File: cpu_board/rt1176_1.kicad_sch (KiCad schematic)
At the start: 81 parts, among them U2 MIMXRT1176, Y3 24.0mHz

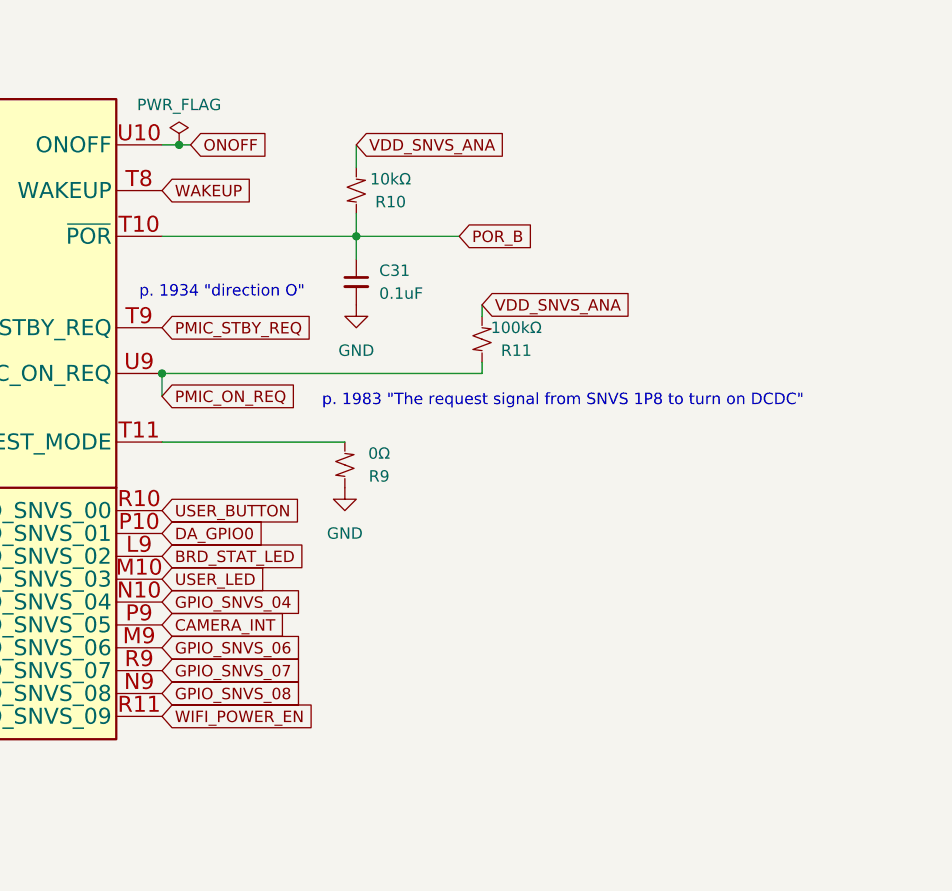
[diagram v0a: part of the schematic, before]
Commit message: clean up board2board connector and organize TODOs
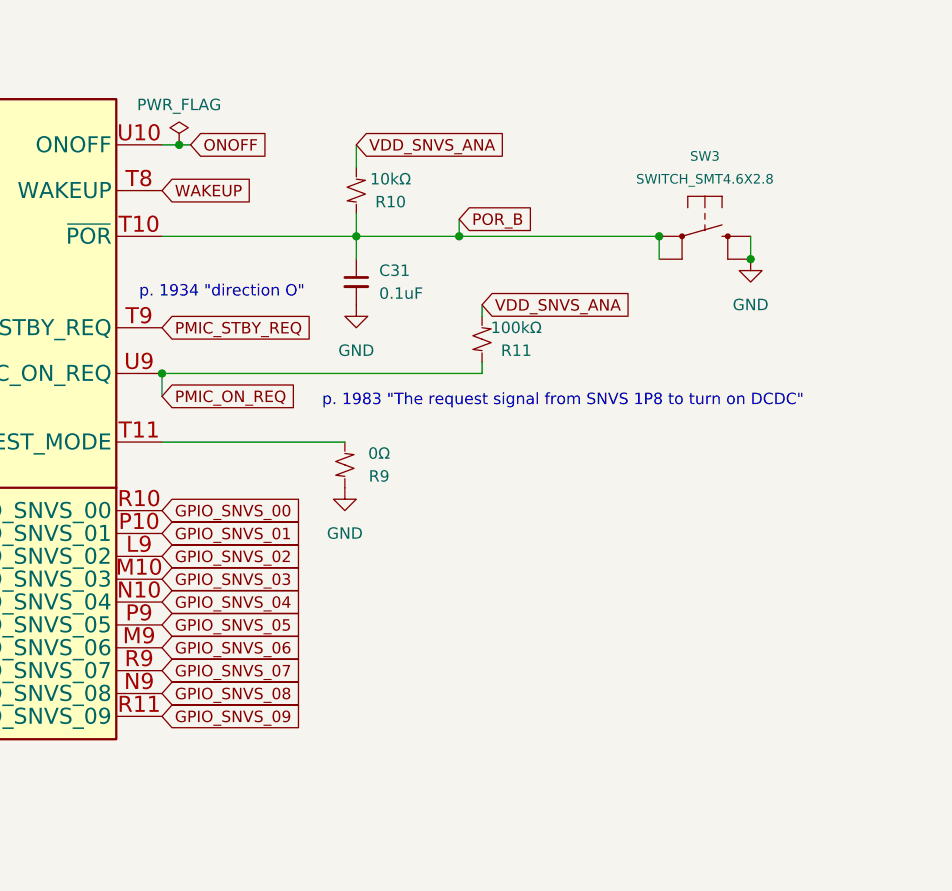
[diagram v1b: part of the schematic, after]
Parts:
- added SW3: SWITCH_SMT4.6X2.8, symbol pycubed_mainboard:SWITCH_SMT4.6X2.8
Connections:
- net GND: now also SW3.B (S), SW3.B' (S1)
- net POR_B: now also SW3.A (P), SW3.A' (P1)
- net BRD_STAT_LED renamed GPIO_SNVS_02
- net CAMERA_INT renamed GPIO_SNVS_05
- net DA_GPIO0 renamed GPIO_SNVS_01
- net USER_BUTTON renamed GPIO_SNVS_00
- net USER_LED renamed GPIO_SNVS_03
- net WIFI_POWER_EN renamed GPIO_SNVS_09
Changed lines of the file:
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@@
   (junction (at 157.48 182.88) (diameter 0) (color 0 0 0 0)
   )
+  (junction (at 304.165 45.72) (diameter 0) (color 0 0 0 0)
+  )
   (junction (at 182.88 48.26) (diameter 0) (color 0 0 0 0)
   )
@@
   (junction (at 152.4 157.48) (diameter 0) (color 0 0 0 0)
   )
+  (junction (at 314.325 48.26) (diameter 0) (color 0 0 0 0)
+  )
   (junction (at 35.56 259.08) (diameter 0) (color 0 0 0 0)
   )
@@
   (junction (at 35.56 241.3) (diameter 0) (color 0 0 0 0)
   )
+  (junction (at 281.94 45.72) (diameter 0) (color 0 0 0 0)
+  )
   (junction (at 66.04 251.46) (diameter 0) (color 0 0 0 0)
   )
@@
     (stroke (width 0) (type default))
   )
+  (wire (pts (xy 281.94 43.815) (xy 281.94 45.72))
+    (stroke (width 0) (type default))
+  )
   (wire (pts (xy 271.78 180.34) (xy 281.94 180.34))
     (stroke (width 0) (type default))
@@
     (stroke (width 0) (type default))
   )
+  (wire (pts (xy 281.94 45.72) (xy 304.165 45.72))
+    (stroke (width 0) (type default))
+  )
   (wire (pts (xy 320.04 129.54) (xy 330.2 129.54))
     (stroke (width 0) (type default))
@@
     (stroke (width 0) (type default))
   )
+  (wire (pts (xy 314.325 45.72) (xy 314.325 48.26))
+    (stroke (width 0) (type default))
+  )
   (wire (pts (xy 246.38 208.28) (xy 246.38 210.82))
     (stroke (width 0) (type default))
@@
     (stroke (width 0) (type default))
   )
+  (wire (pts (xy 304.165 45.72) (xy 304.165 48.26))
+    (stroke (width 0) (type default))
+  )
   (wire (pts (xy 152.4 157.48) (xy 162.56 157.48))
     (stroke (width 0) (type default))
@@
     )
   )
-  (global_label "USER_BUTTON" (shape input) (at 248.92 76.2 0) (fields_autoplaced)
+  (global_label "GPIO_SNVS_00" (shape input) (at 248.92 76.2 0) (fields_autoplaced)
     (effects (font (size 1.27 1.27)) (justify left))
-    (property "Intersheetrefs" "${INTERSHEET_REFS}" (at 265.0285 76.2 0)
+    (property "Intersheetrefs" "${INTERSHEET_REFS}" (at 265.5728 76.2 0)
       (effects (font (size 1.27 1.27)) (justify left) hide)
     )
   )
-  (global_label "CAMERA_INT" (shape input) (at 248.92 88.9 0) (fields_autoplaced)
+  (global_label "GPIO_SNVS_05" (shape input) (at 248.92 88.9 0) (fields_autoplaced)
     (effects (font (size 1.27 1.27)) (justify left))
-    (property "Intersheetrefs" "${INTERSHEET_REFS}" (at 263.0933 88.9 0)
+    (property "Intersheetrefs" "${INTERSHEET_REFS}" (at 265.5728 88.9 0)
       (effects (font (size 1.27 1.27)) (justify left) hide)
     )
@@
     )
   )
-  (global_label "DA_GPIO0" (shape input) (at 248.92 78.74 0) (fields_autoplaced)
+  (global_label "GPIO_SNVS_01" (shape input) (at 248.92 78.74 0) (fields_autoplaced)
     (effects (font (size 1.27 1.27)) (justify left))
-    (property "Intersheetrefs" "${INTERSHEET_REFS}" (at 260.9162 78.74 0)
+    (property "Intersheetrefs" "${INTERSHEET_REFS}" (at 265.5728 78.74 0)
       (effects (font (size 1.27 1.27)) (justify left) hide)
     )
@@
     )
   )
-  (global_label "WIFI_POWER_EN" (shape input) (at 248.92 99.06 0) (fields_autoplaced)
+  (global_label "GPIO_SNVS_09" (shape input) (at 248.92 99.06 0) (fields_autoplaced)
     (effects (font (size 1.27 1.27)) (justify left))
-    (property "Intersheetrefs" "${INTERSHEET_REFS}" (at 266.5404 99.06 0)
+    (property "Intersheetrefs" "${INTERSHEET_REFS}" (at 265.5728 99.06 0)
       (effects (font (size 1.27 1.27)) (justify left) hide)
     )
@@
     )
   )
-  (global_label "BRD_STAT_LED" (shape input) (at 248.92 81.28 0) (fields_autoplaced)
+  (global_label "GPIO_SNVS_02" (shape input) (at 248.92 81.28 0) (fields_autoplaced)
     (effects (font (size 1.27 1.27)) (justify left))
-    (property "Intersheetrefs" "${INTERSHEET_REFS}" (at 265.3308 81.28 0)
+    (property "Intersheetrefs" "${INTERSHEET_REFS}" (at 265.5728 81.28 0)
       (effects (font (size 1.27 1.27)) (justify left) hide)
     )
@@
     )
   )
-  (global_label "POR_B" (shape input) (at 281.94 45.72 0) (fields_autoplaced)
+  (global_label "POR_B" (shape input) (at 281.94 43.815 0) (fields_autoplaced)
     (effects (font (size 1.27 1.27)) (justify left))
-    (property "Intersheetrefs" "${INTERSHEET_REFS}" (at 291.0333 45.72 0)
+    (property "Intersheetrefs" "${INTERSHEET_REFS}" (at 291.0333 43.815 0)
       (effects (font (size 1.27 1.27)) (justify left) hide)
     )
@@
     )
   )
-  (global_label "USER_LED" (shape input) (at 248.92 83.82 0) (fields_autoplaced)
+  (global_label "GPIO_SNVS_03" (shape input) (at 248.92 83.82 0) (fields_autoplaced)
     (effects (font (size 1.27 1.27)) (justify left))
-    (property "Intersheetrefs" "${INTERSHEET_REFS}" (at 261.2789 83.82 0)
+    (property "Intersheetrefs" "${INTERSHEET_REFS}" (at 265.5728 83.82 0)
       (effects (font (size 1.27 1.27)) (justify left) hide)
     )
@@
     )
   )
+  (symbol (lib_id "power:GND") (at 314.325 48.26 0) (unit 1)
+    (in_bom yes) (on_board yes) (dnp no) (fields_autoplaced)
+    (property "Reference" "#PWR068" (at 314.325 54.61 0)
+      (effects (font (size 1.27 1.27)) hide)
+    )
+    (property "Value" "GND" (at 314.325 53.34 0)
+      (effects (font (size 1.27 1.27)))
+    )
+    (property "Footprint" "" (at 314.325 48.26 0)
+      (effects (font (size 1.27 1.27)) hide)
+    )
+    (property "Datasheet" "" (at 314.325 48.26 0)
+      (effects (font (size 1.27 1.27)) hide)
+    )
+    (pin "1")
+    (instances
+      (project "cpu_board"
+        (path "/c4fd7bdd-408e-44be-b66f-e6a18a0ca6e3/9cbcd73e-afcb-4ff3-8583-4372f7e826ca"
+          (reference "#PWR068") (unit 1)
+        )
+      )
+    )
+  )
   (symbol (lib_id "Device:C_Small") (at 162.56 160.02 0) (unit 1)
     (in_bom yes) (on_board yes) (dnp no) (fields_autoplaced)
@@
         )
       )
+    )
+  )
+  (symbol (lib_id "pycubed_mainboard:SWITCH_SMT4.6X2.8") (at 309.245 45.72 0) (unit 1)
+    (in_bom yes) (on_board yes) (dnp no) (fields_autoplaced)
+    (property "Reference" "SW3" (at 309.245 36.83 0)
+      (effects (font (size 1.0668 1.0668)))
+    )
+    (property "Value" "SWITCH_SMT4.6X2.8" (at 309.245 39.37 0)
+      (effects (font (size 1.0668 1.0668)))
+    )
+    (property "Footprint" "" (at 309.245 45.72 0)
+      (effects (font (size 1.27 1.27)) hide)
+    )
+    (property "Datasheet" "" (at 309.245 45.72 0)
+      (effects (font (size 1.27 1.27)) hide)
+    )
+    (pin "A")
+    (pin "A'")
+    (pin "B")
+    (pin "B'")
+    (instances
+      (project "cpu_board"
+        (path "/c4fd7bdd-408e-44be-b66f-e6a18a0ca6e3/9cbcd73e-afcb-4ff3-8583-4372f7e826ca"
+          (reference "SW3") (unit 1)
+        )
+      )

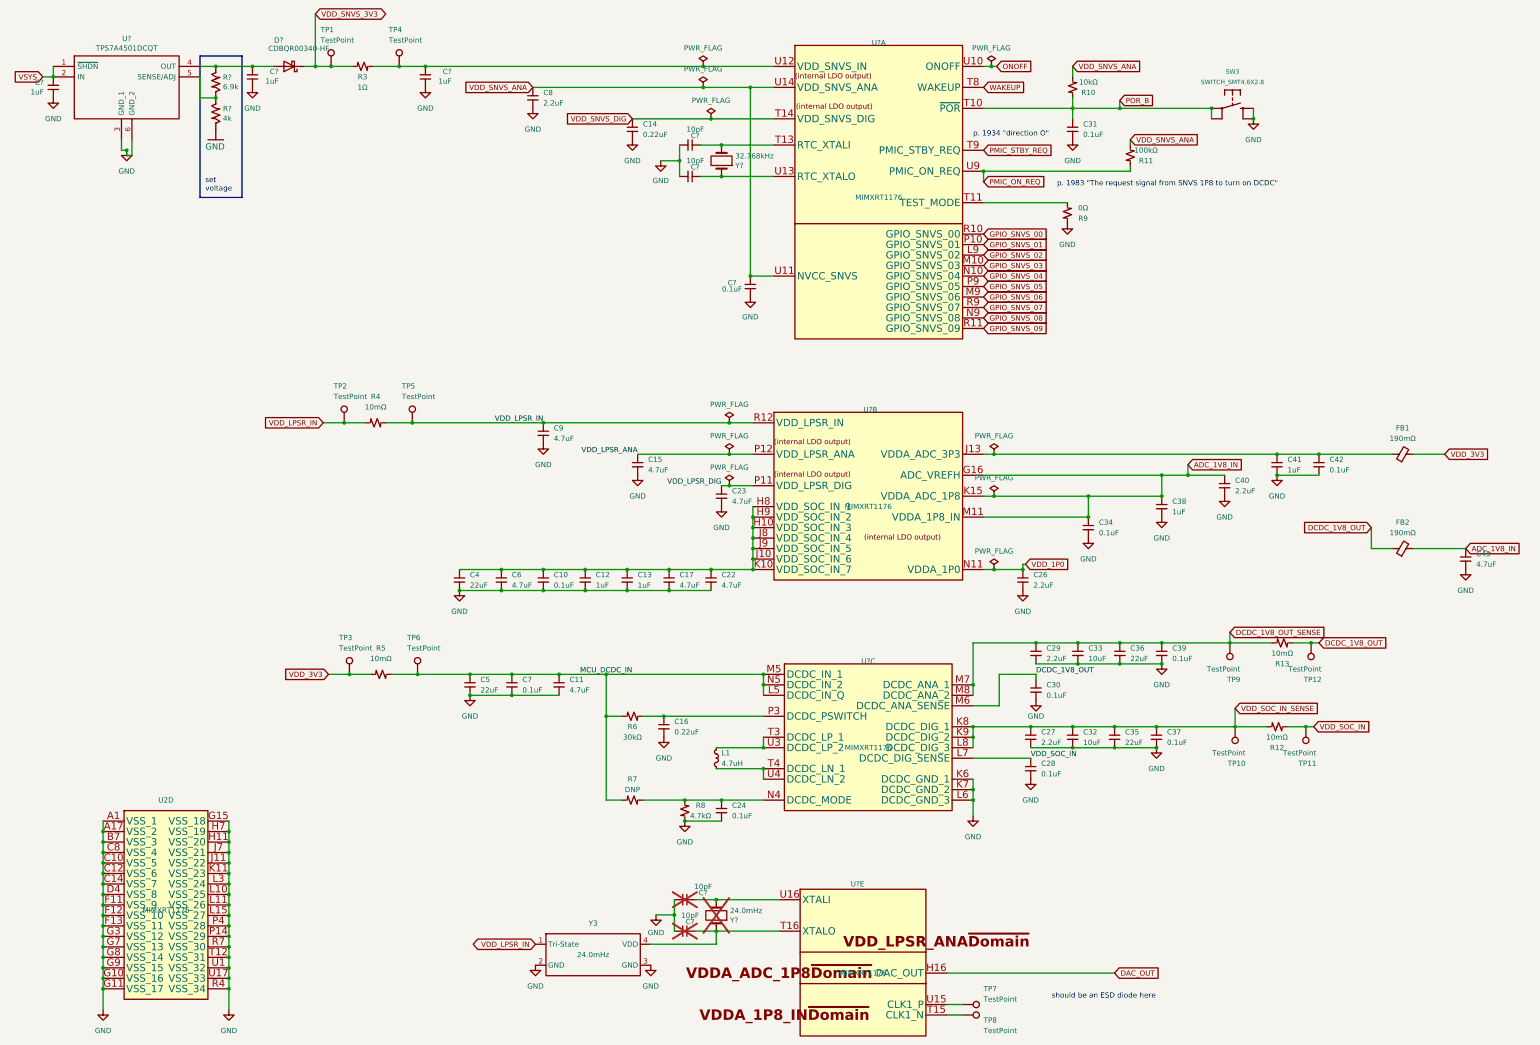
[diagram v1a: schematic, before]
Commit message: route most of power distribution
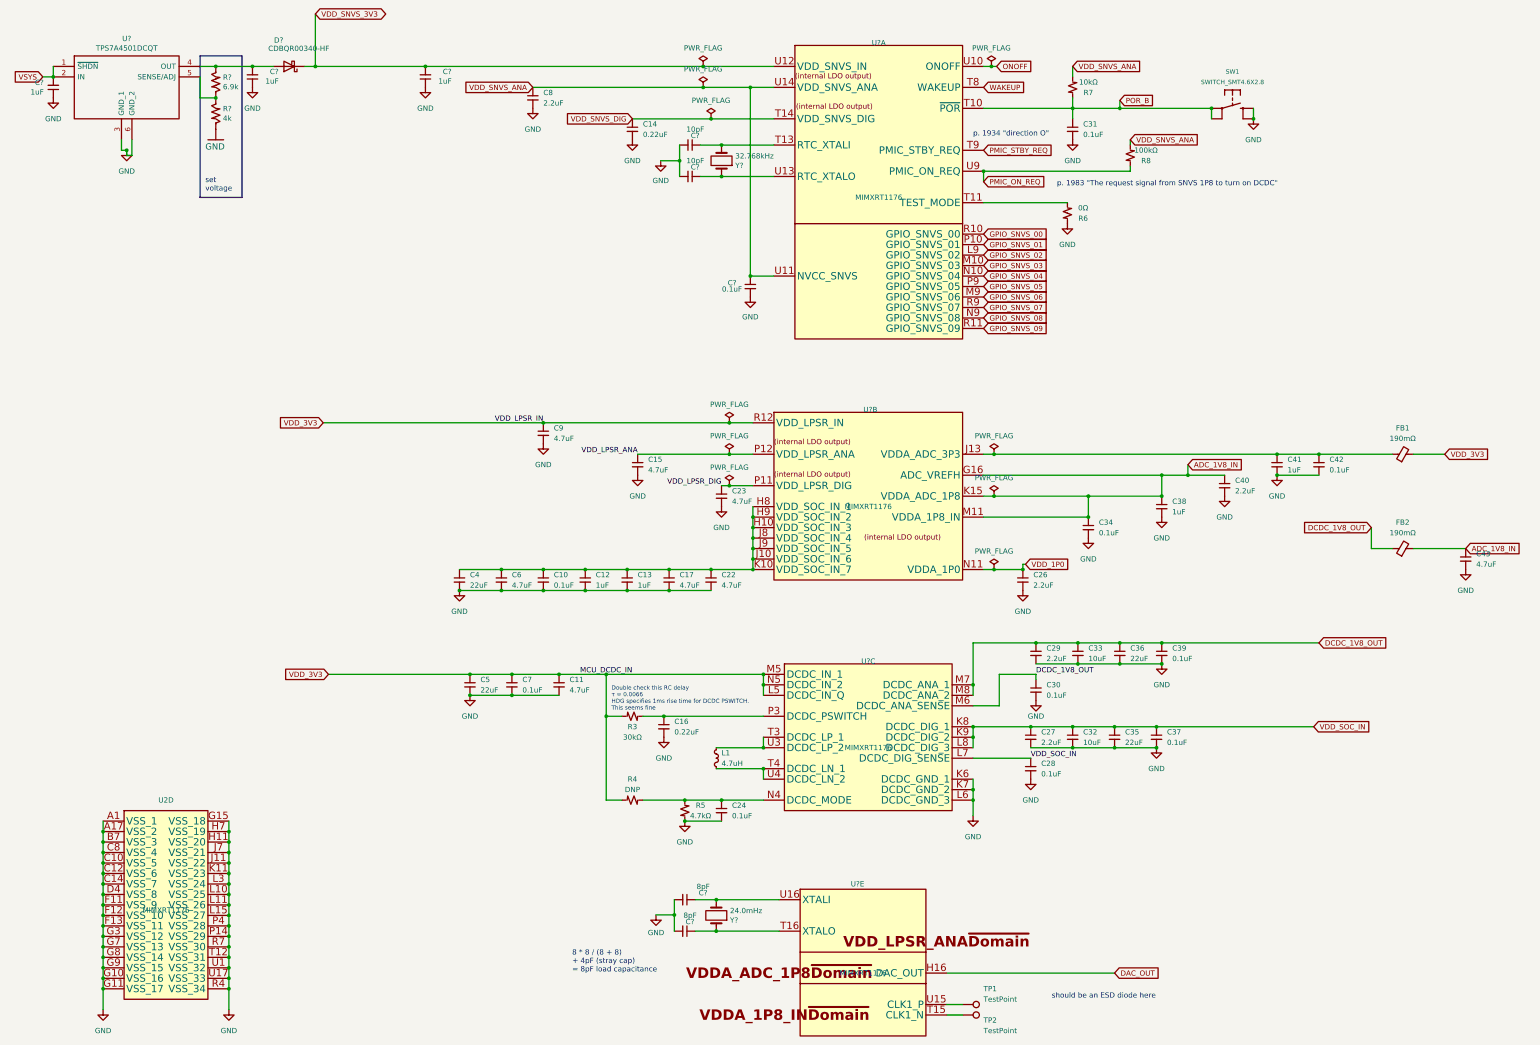
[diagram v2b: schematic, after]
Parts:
- removed R12, R13, R4, R5: 10mΩ, Resistor_SMD:R_0603_1608Metric, symbol Device:R_Small_US
- removed R3: 1Ω, Resistor_SMD:R_0603_1608Metric, symbol Device:R_Small_US
- removed TP1, TP10, TP11, TP12, TP2, TP3, TP4, TP5, TP6, TP9: TestPoint, TestPoint:TestPoint_Pad_1.5x1.5mm, symbol Connector:TestPoint
- removed Y3: 24.0mHz, adcs:OSC-SMD_4P-L2.5-W2.0-BL, symbol adcs:TCXO
- C? (x2): value 10pF -> 8pF; now fitted
- SW1: renamed from SW3; footprint (none) -> mainboard:BTN_KMR2_4.6X2.8
- TP1: renamed from TP7; footprint TestPoint:TestPoint_Pad_1.5x1.5mm -> TestPoint:TestPoint_Pad_1.0x1.0mm; JLCPCB P/N (none) -> C221678
- TP2: renamed from TP8; footprint TestPoint:TestPoint_Pad_1.5x1.5mm -> TestPoint:TestPoint_Pad_1.0x1.0mm; JLCPCB P/N (none) -> C221678
- Y?: Flight XRCGB24M000F1SBDR0 -> XRCGB24M000F1H01R0; JLCPCB P/N (none) -> C1986107; now fitted
- renumbered R6 to R3, R7 to R4, R8 to R5, R9 to R6, R10 to R7, R11 to R8
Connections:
- net DCDC_1V8_OUT_SENSE is gone; now on net DCDC_1V8_OUT: C29.1, C33.1, C36.1, C39.1, U?.M7 (DCDC_ANA_1), U?.M8 (DCDC_ANA_2)
- net MCU_DCDC_IN is gone; now on net VDD_3V3: C11.1, C5.1, C7.1, R3.1, R4.2, U?.L5 (DCDC_IN_Q), U?.M5 (DCDC_IN_1), U?.N5 (DCDC_IN_2)
- net VDD_LPSR_IN is gone; now on net VDD_3V3: C9.1, U?.R12 (VDD_LPSR_IN)
- net VDD_SOC_IN_SENSE is gone; now on net VDD_SOC_IN: C27.1, C32.1, C35.1, C37.1, U?.K8 (DCDC_DIG_1), U?.K9 (DCDC_DIG_2), U?.L8 (DCDC_DIG_3)
- net VDD_SNVS_3V3: now also C?.2, U?.U12 (VDD_SNVS_IN)
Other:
- note added: "8 * 8 / (8 + 8) + 4pF (stray cap) = 8pF load capacitance"
- note added: "Double check this RC delay τ = 0.0066 HDG specifies 1ms rise time for DCDC PSWITCH. This seems fine"

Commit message: floorplan complete
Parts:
- removed C11: 4.7uF, Capacitor_SMD:C_0402_1005Metric, symbol Device:C_Small
- removed C16: 0.22uF, Capacitor_SMD:C_0402_1005Metric, symbol Device:C_Small
- removed C24, C28, C30, C37, C39, C7: 0.1uF, Capacitor_SMD:C_0402_1005Metric, symbol Device:C_Small
- removed C27, C29: 2.2uF, Capacitor_SMD:C_0402_1005Metric, symbol Device:C_Small
- removed C32, C33: 10uF, Capacitor_SMD:C_0402_1005Metric, symbol Device:C_Small
- removed C35, C36, C5: 22uF, Capacitor_SMD:C_0402_1005Metric, symbol Device:C_Small
- removed L1: 4.7uH, adcs:IND-SMD_L5.8-W5.2_PIO54, symbol Device:L_Small
- removed R3: 30kΩ, Resistor_SMD:R_0402_1005Metric, symbol Device:R_Small_US
- removed R4: DNP, Resistor_SMD:R_0402_1005Metric, symbol Device:R_Small_US
- removed R5: 4.7kΩ, Resistor_SMD:R_0402_1005Metric, symbol Device:R_Small_US
- removed R6: 0Ω, Resistor_SMD:R_0402_1005Metric, symbol Device:R_Small_US
- FB1, FB2: footprint adcs:L0402_H0.55MM -> Inductor_SMD:L_0402_1005Metric
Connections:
- net ADC_1V8_IN: no longer C34.1, U?.M11 (VDDA_1P8_IN)
- net GND: now also U?.N4 (DCDC_MODE), U?.P3 (DCDC_PSWITCH), U?.T11 (TEST_MODE)
- net VDD_3V3: no longer U?.L5 (DCDC_IN_Q), U?.M5 (DCDC_IN_1), U?.N5 (DCDC_IN_2)
- net VDD_SOC_IN: now also C10.1, C12.1, C13.1, C17.1, C22.1, C4.1, C6.1, U?.H10 (VDD_SOC_IN_3), U?.H8 (VDD_SOC_IN_1), U?.H9 (VDD_SOC_IN_2), U?.J10 (VDD_SOC_IN_6), U?.J8 (VDD_SOC_IN_4), U?.J9 (VDD_SOC_IN_5), U?.K10 (VDD_SOC_IN_7); no longer U?.K8 (DCDC_DIG_1), U?.K9 (DCDC_DIG_2), U?.L7 (DCDC_DIG_SENSE), U?.L8 (DCDC_DIG_3)
- net VDDA_ADC_3P3: now reaches C41.1, C42.1, FB1.1, U?.J13 (VDDA_ADC_3P3)
- net at U?.T3 (DCDC_LP_1): no longer U?.U3 (DCDC_LP_2)
- net at U?.T4 (DCDC_LN_1): no longer U?.U4 (DCDC_LN_2)
- net CLK1_P: now reaches TP1.1, U?.U15 (CLK1_P)
- net CLK1_N: now reaches TP2.1, U?.T15 (CLK1_N)
- removed net DCDC_1V8_OUT: FB2.1, U?.M6 (DCDC_ANA_SENSE), U?.M7 (DCDC_ANA_1), U?.M8 (DCDC_ANA_2)
- new net: C34.1, U?.M11 (VDDA_1P8_IN)
- new net VDD_1V8: FB2.1
- no-connect marks 0 -> 14
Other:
- note added: "HDUG says this should be 1uF"
- note added: "Not using internal regulators. HDUG page 6."
- note added: "p. 1983 "The request signal from SNVS 1P8 to turn on DCDC". We do not use DCDC regs inside the chip"
- note removed: "Double check this RC delay τ = 0.0066 HDG specifies 1ms rise time for DCDC PSWITCH. This seems fine"
- note removed: "p. 1983 "The request signal from SNVS 1P8 to turn on DCDC""
